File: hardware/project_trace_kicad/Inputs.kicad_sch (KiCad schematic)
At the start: 41 parts, among them J201 Conn_01x01_Socket, J202 Conn_01x01_Socket, J203 Conn_01x01_Socket, J204 Screw_Terminal_01x04, J205 Conn_Coaxial, U201 TLE2426xLP, U202 AQW280SX, U203 AQW282SX, U204 OPA2837IRUNT, U205 TS5A23159DGS, U206 OPA2837IRUNT

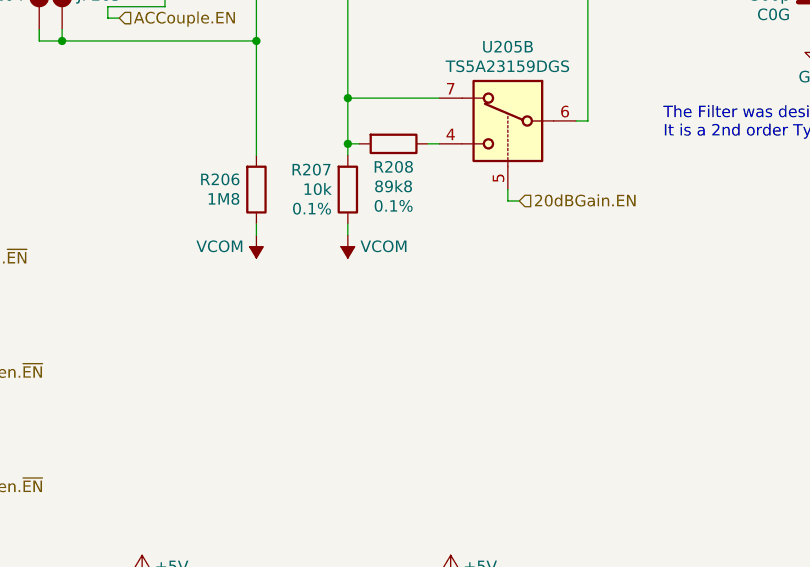
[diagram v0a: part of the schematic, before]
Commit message: Fix Bug in Diffamp, update PCB
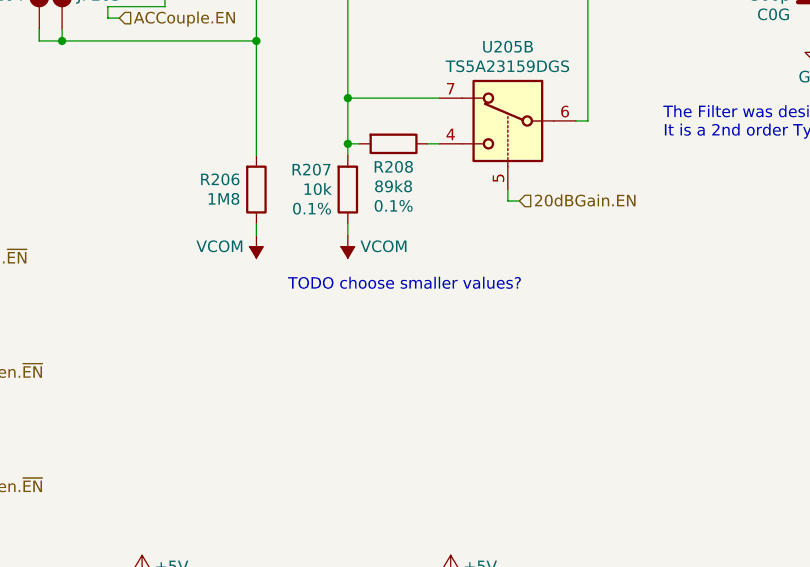
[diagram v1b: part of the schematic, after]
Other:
- note added: "TODO choose smaller values?"
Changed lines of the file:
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@@
+		)
+	)
+	(text "TODO choose smaller values?"
+		(exclude_from_sim no)
+		(at 186.69 102.108 0)
+		(effects
+			(font
+				(size 1.27 1.27)
+			)
 		)
 	)

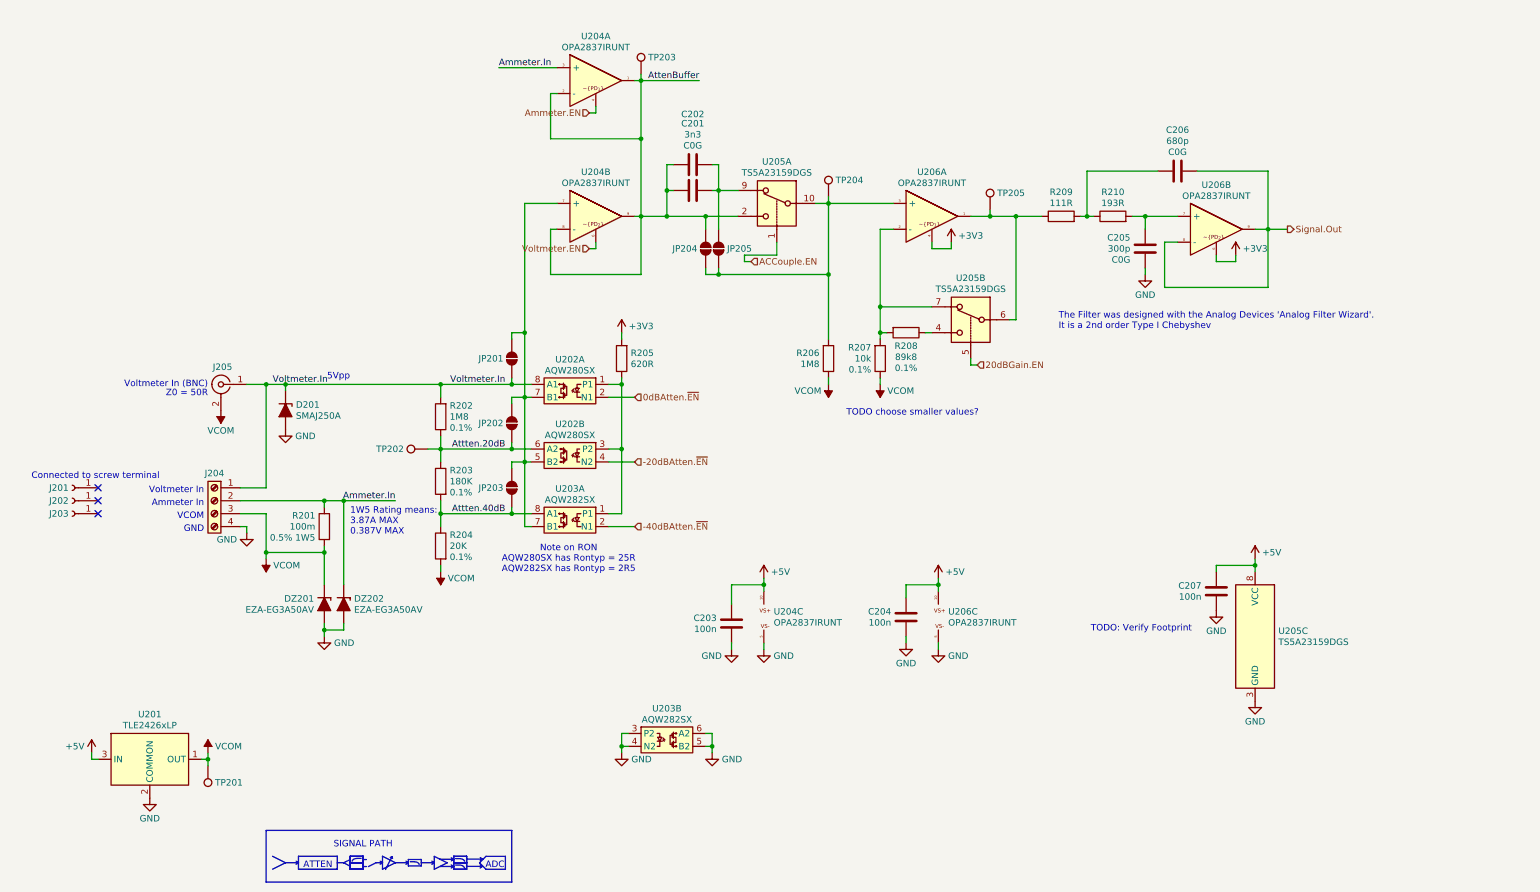
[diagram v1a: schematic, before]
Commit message: Work on PCB, Fix bugs, Improve noise performance
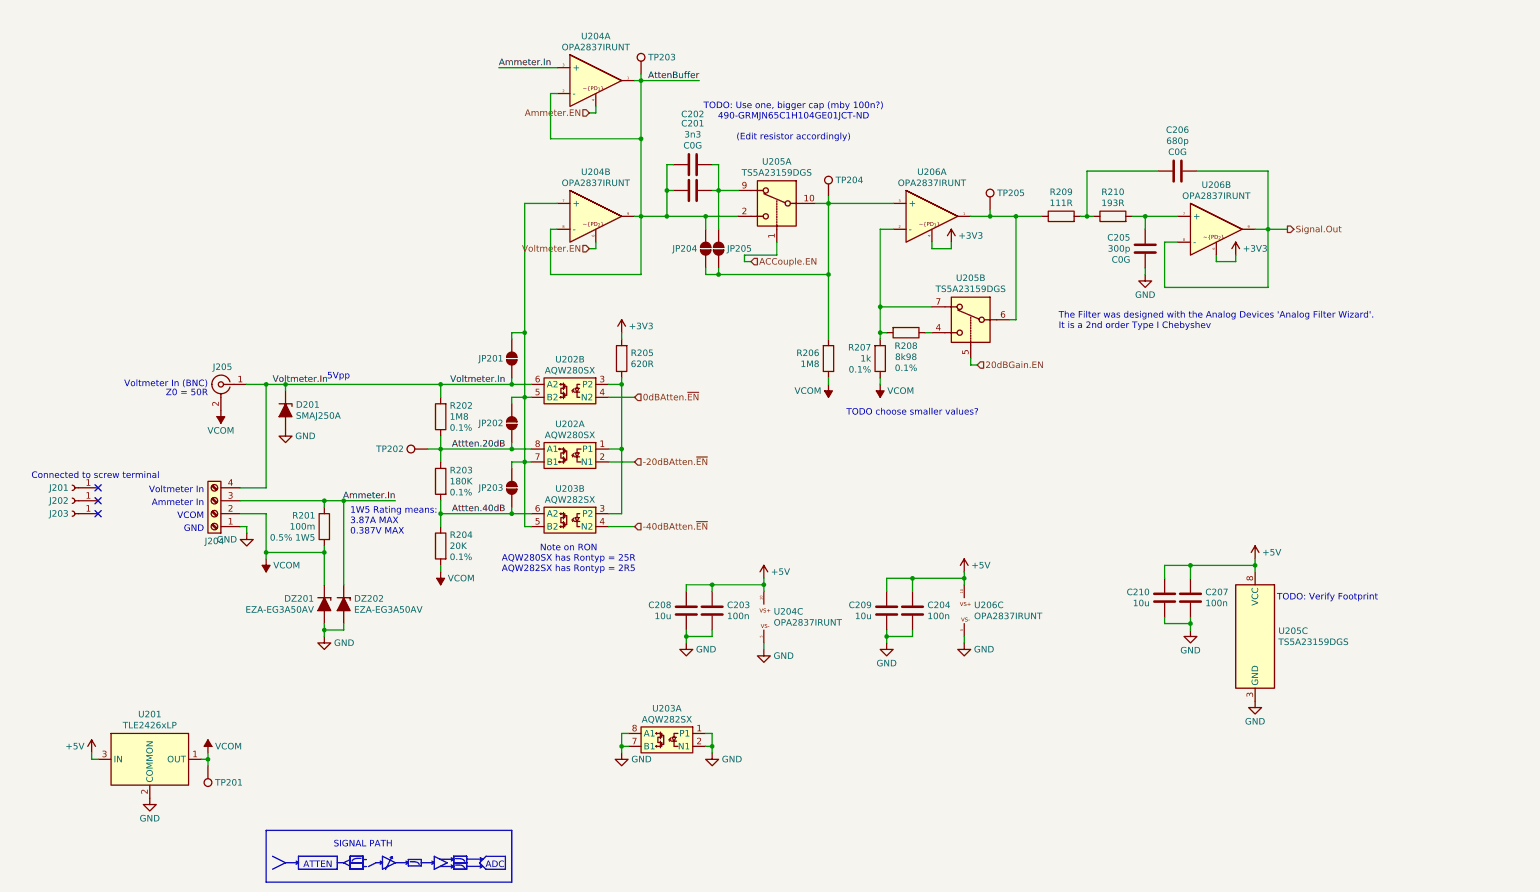
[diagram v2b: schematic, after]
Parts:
- added C208, C209, C210: 10u, Capacitor_SMD:C_0805_2012Metric_Pad1.18x1.45mm_HandSolder, symbol Device:C
- R207: value 10k -> 1k; DigikeyPN YAG1236CT-ND -> (none)
- R208: value 89k8 -> 8k98; DigikeyPN YAG1236CT-ND -> (none)
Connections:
- net +5V: now also C208.2, C209.2, C210.2
- net -20dBAtten.~{EN}: now also U202.2 (N1); no longer U202.4 (N2)
- net -40dBAtten.~{EN}: now also U203.4 (N2); no longer U203.2 (N1)
- net 0dBAtten.~{EN}: now also U202.4 (N2); no longer U202.2 (N1)
- net Ammeter.In: now also J204.3 (Pin_3); no longer J204.2 (Pin_2)
- net Attten.20dB: now also U202.8 (A1); no longer U202.6 (A2)
- net Attten.40dB: now also U203.6 (A2); no longer U203.8 (A1)
- net GND: now also J204.1 (Pin_1), U203.1 (P1), U203.2 (N1), U203.7 (B1), U203.8 (A1), C208.1, C209.1, C210.1; no longer J204.4 (Pin_4), U203.3 (P2), U203.4 (N2), U203.5 (B2), U203.6 (A2)
- net VCOM: now also J204.2 (Pin_2); no longer J204.3 (Pin_3)
- net Voltmeter.In: now also J204.4 (Pin_4), U202.6 (A2); no longer J204.1 (Pin_1), U202.8 (A1)
- net at R205.1, U202.1 (P1), U202.3 (P2): now also U203.3 (P2); no longer U203.1 (P1)
- net at JP201.2 (B), JP202.2 (B), JP203.2 (B)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: now also U203.5 (B2); no longer U203.7 (B1)
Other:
- note added: "TODO: Use one, bigger cap (mby 100n?) 490-GRMJN65C1H104GE01JCT-ND (Edit resistor accordingly)"
- moved on the sheet: C203, C204, C207, J204, U202A, U202B, U203A, U203B, U206C

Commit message: Layout Broad Strokes, Fix STM32H7 Error
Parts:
- added C211: 10u, Capacitor_SMD:C_0805_2012Metric_Pad1.18x1.45mm_HandSolder, symbol Device:C
- added C212: 100n, Capacitor_SMD:C_0603_1608Metric_Pad1.08x0.95mm_HandSolder, symbol Device:C
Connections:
- net +5V: now also C211.2, C212.1
- net 20dBGain.EN: now also U205.1; no longer U205.5
- net ACCouple.EN: now also U205.5; no longer U205.1
- net AttenBuffer: now also U205.4; no longer U205.2
- net GND: now also C211.1, C212.2
- net at JP204.2 (B), JP205.2 (B), TP204.1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: now also U205.6; no longer R206.2, U205.10
- net at R209.1, TP205.1, U206.1: now also U205.10; no longer U205.6
- net at R207.2, R208.2, U206.2 (-): now also U205.9; no longer U205.7
- net at R208.1: now also U205.2; no longer U205.4
- net at C201.2, C202.2, JP205.1 (A): now also R206.2, U205.7; no longer U205.9
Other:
- moved on the sheet: R206, U205A, U205B

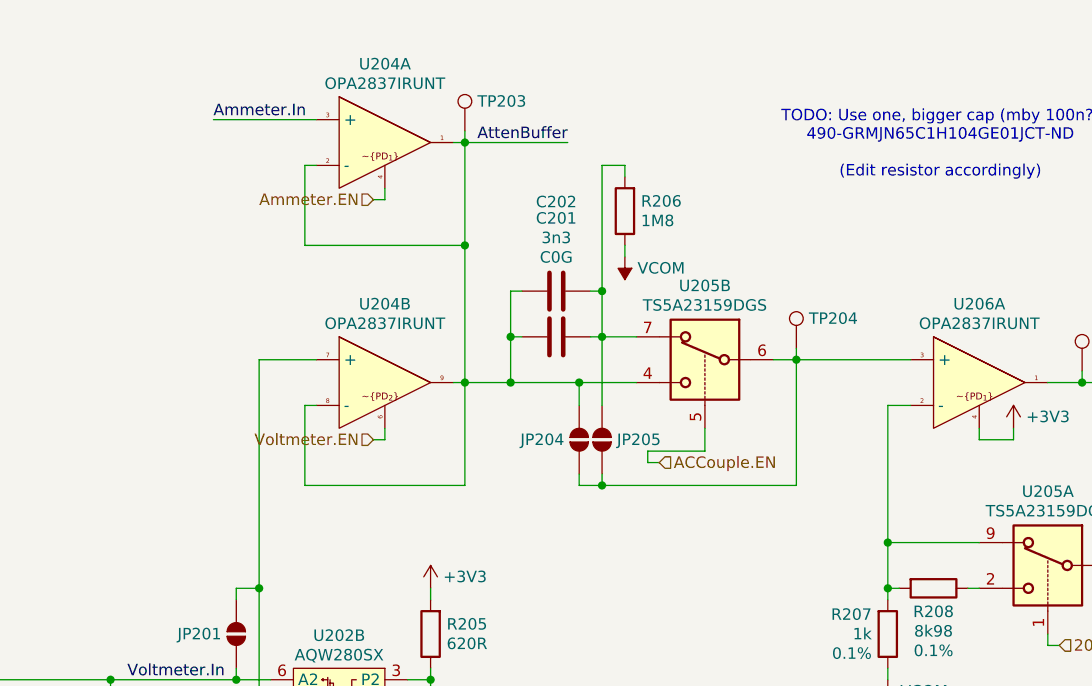
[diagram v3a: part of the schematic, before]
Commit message: Add missing Part-numers, Revise AC Coupling
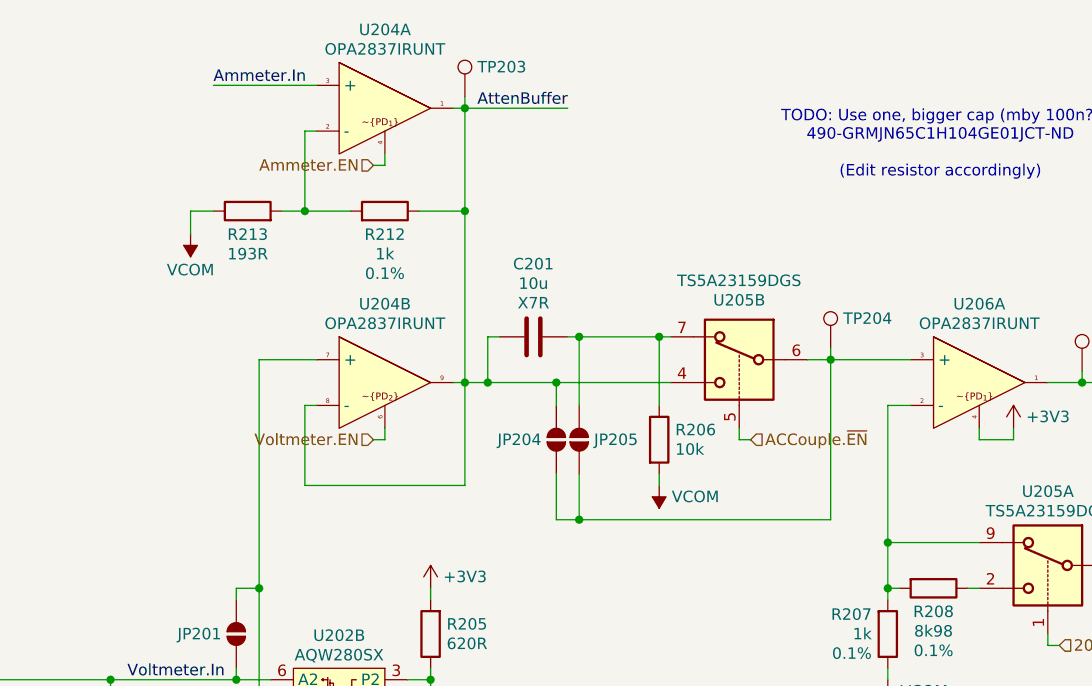
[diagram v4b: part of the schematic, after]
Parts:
- removed C202: 3n3, Capacitor_SMD:C_0603_1608Metric_Pad1.08x0.95mm_HandSolder, symbol Device:C
- added R212: 1k, Resistor_SMD:R_0603_1608Metric_Pad0.98x0.95mm_HandSolder, symbol Device:R
- added R213: 193R, Resistor_SMD:R_0603_1608Metric_Pad0.98x0.95mm_HandSolder, symbol Device:R
- C201: value 3n3 -> 10u; footprint Capacitor_SMD:C_0603_1608Metric_Pad1.08x0.95mm_HandSolder -> Capacitor_SMD:C_0805_2012Metric_Pad1.18x1.45mm_HandSolder; DigikeyPN 490-GCM1885C1H332FA16DCT-ND -> 490-10516-1-ND; Extra C0G -> X7R
- C205: DigikeyPN (none) -> 311-3967-1-ND
- C206: DigikeyPN (none) -> 311-1425-1-ND
- R206: value 1M8 -> 10k; footprint Resistor_SMD:R_0805_2012Metric_Pad1.20x1.40mm_HandSolder -> Resistor_SMD:R_0603_1608Metric_Pad0.98x0.95mm_HandSolder; DigikeyPN 408-2026-1-ND -> YAG1236CT-ND; Extra 0.1% -> (none)
- R207: DigikeyPN (none) -> YAG1237CT-ND
- R208: DigikeyPN (none) -> 13-RT0603BRD078K98LCT-ND
- R209: DigikeyPN (none) -> 2019-RN73R1JTTD1110B25CT-ND
- R210: DigikeyPN (none) -> 13-RT0603DRE07193RLCT-ND
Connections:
- net AttenBuffer: now also C201.2, R212.1; no longer C201.1, U204.2 (-)
- net VCOM: now also R206.2, R213.1; no longer R206.1
- net at JP205.1 (A), U205.7: now also C201.1, R206.1; no longer C201.2, R206.2
- net ACCouple.EN renamed ACCouple.~{EN}
- new net: R212.2, R213.2, U204.2 (-)
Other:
- moved on the sheet: JP204, JP205, TP203, TP204, U204A, U205B

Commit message: Address Review Comments
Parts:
- added C202: 4u7, Capacitor_THT:CP_Radial_D6.3mm_P2.50mm, symbol Device:C_Polarized
- added C213: 100n, Capacitor_SMD:C_0603_1608Metric_Pad1.08x0.95mm_HandSolder, symbol Device:C
- added U207: SN74LVC2G14DBV, Package_TO_SOT_SMD:SOT-23-6_Handsoldering, symbol 74xGxx:SN74LVC2G14DBV
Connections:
- net Ammeter.EN: now also U207.6 (1Y)
- net GND: now also C202.2, C213.2, U207.2 (GND), U207.3 (2A)
- net VCOM: now also C202.1
- net Voltmeter.EN: now also U207.1 (1A)
- new net: C213.1, U207.5 (V_{CC})
- no-connect marks 3 -> 4
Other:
- note added: "AC/DC Coupling"
- note added: "ADC has its nyquist frequency at 20MHz as it uses oversampling and a digital anti-aliasing filter."
- note added: "Attenuator"
- note added: "Sallen-Key Antialiasing Filter"
- note added: "Switchable Gain Amplifier"
- note added: "TODO: Connect new ammeter.en"
- note removed: "TODO: Use one, bigger cap (mby 100n?) 490-GRMJN65C1H104GE01JCT-ND (Edit resistor accordingly)"
- moved on the sheet: TP201

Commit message: Updates to PCB, Schematic Fixes
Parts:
- U207: DigikeyPN (none) -> 296-13010-1-ND
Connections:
- net +3V3: now also C213.1, U207.5 (V_{CC})
- net Voltmeter.EN renamed VOLT/~{AMP}
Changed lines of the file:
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@@
 	)
 	(junction
+		(at 67.31 31.75)
+		(diameter 0)
+		(color 0 0 0 0)
+	)
+	(junction
 		(at 129.54 167.64)
 		(diameter 0)
@@
 	(wire
 		(pts
-			(xy 105.41 30.48) (xy 116.84 30.48)
+			(xy 102.87 30.48) (xy 116.84 30.48)
 		)
 		(stroke
@@
 	(wire
 		(pts
-			(xy 124.46 69.85) (xy 124.46 68.58)
+			(xy 124.46 71.12) (xy 124.46 68.58)
 		)
 		(stroke
@@
 	(wire
 		(pts
-			(xy 124.46 39.37) (xy 124.46 38.1)
+			(xy 124.46 38.1) (xy 124.46 41.91)
 		)
 		(stroke
@@
 	(wire
 		(pts
-			(xy 123.19 69.85) (xy 124.46 69.85)
+			(xy 123.19 71.12) (xy 124.46 71.12)
 		)
 		(stroke
@@
 	(wire
 		(pts
+			(xy 67.31 30.48) (xy 67.31 31.75)
+		)
+		(stroke
+			(width 0)
+			(type default)
+		)
+	)
+	(wire
+		(pts
 			(xy 182.88 66.04) (xy 180.34 66.04)
 		)
@@
 	(wire
 		(pts
+			(xy 102.87 41.91) (xy 124.46 41.91)
+		)
+		(stroke
+			(width 0)
+			(type default)
+		)
+	)
+	(wire
+		(pts
 			(xy 129.54 168.91) (xy 129.54 167.64)
 		)
@@
 	(wire
 		(pts
-			(xy 124.46 39.37) (xy 123.19 39.37)
-		)
-		(stroke
-			(width 0)
-			(type default)
-		)
-	)
-	(wire
-		(pts
 			(xy 107.95 96.52) (xy 111.76 96.52)
 		)
@@
 		)
 	)
+	(label "Ammeter.EN"
+		(at 102.87 41.91 0)
+		(effects
+			(font
+				(size 1.27 1.27)
+			)
+			(justify left bottom)
+		)
+	)
 	(label "Ammeter.In"
 		(at 85.09 119.38 180)
@@
 	)
 	(label "Ammeter.In"
-		(at 105.41 30.48 0)
+		(at 102.87 30.48 0)
 		(effects
 			(font
@@
 		)
 	)
-	(hierarchical_label "Ammeter.EN"
-		(shape input)
-		(at 123.19 39.37 180)
-		(effects
-			(font
-				(size 1.27 1.27)
-			)
-			(justify right)
-		)
-	)
 	(hierarchical_label "-40dBAtten.~{EN}"
 		(shape input)
@@
 		)
 	)
-	(hierarchical_label "Voltmeter.EN"
-		(shape input)
-		(at 123.19 69.85 180)
-		(effects
-			(font
-				(size 1.27 1.27)
-			)
-			(justify right)
-		)
-	)
 	(hierarchical_label "Signal.Out"
 		(shape output)
@@
 		)
 	)
-	(hierarchical_label "Voltmeter.EN"
+	(hierarchical_label "VOLT{slash}~{AMP}"
+		(shape input)
+		(at 123.19 71.12 180)
+		(effects
+			(font
+				(size 1.27 1.27)
+			)
+			(justify right)
+		)
+	)
+	(hierarchical_label "VOLT{slash}~{AMP}"
 		(shape input)
 		(at 55.88 50.8 180)
@@
 			)
 		)
+		(property "DigikeyPN" "296-13010-1-ND"
+			(at 67.31 53.34 0)
+			(hide yes)
+			(show_name no)
+			(do_not_autoplace no)
+			(effects
+				(font
+					(size 1.27 1.27)
+				)
+			)
+		)
 		(pin "5"
 		)
@@
 				)
 			)
+		)
+	)
+	(symbol
+		(lib_id "power:+3V3")
+		(at 67.31 30.48 0)
+		(unit 1)
+		(body_style 1)
+		(exclude_from_sim no)
+		(in_bom yes)
+		(on_board yes)
+		(in_pos_files yes)
+		(dnp no)
+		(fields_autoplaced yes)
+		(property "Reference" "#PWR0233"
+			(at 67.31 34.29 0)
+			(hide yes)
+			(show_name no)
+			(do_not_autoplace no)
+			(effects
+				(font
+					(size 1.27 1.27)
+				)
+			)
+		)
+		(property "Value" "+3V3"
+			(at 67.31 26.4752 0)
+			(show_name no)
+			(do_not_autoplace no)
+			(effects
+				(font
+					(size 1.27 1.27)
+				)
+			)
+		)
+		(property "Footprint" ""
+			(at 67.31 30.48 0)
+			(hide yes)
+			(show_name no)
+			(do_not_autoplace no)
+			(effects
+				(font
+					(size 1.27 1.27)
+				)
+			)
+		)
+		(property "Datasheet" ""
+			(at 67.31 30.48 0)
+			(hide yes)
+			(show_name no)
+			(do_not_autoplace no)
+			(effects
+				(font
+					(size 1.27 1.27)
+				)
+			)
+		)
+		(property "Description" "Power symbol creates a global label with name \"+3V3\""
+			(at 67.31 30.48 0)
+			(hide yes)
+			(show_name no)
+			(do_not_autoplace no)
+			(effects
+				(font
+					(size 1.27 1.27)
+				)
+			)
+		)
+		(pin "1"
+		)
+		(instances
+			(project "project_trace_kicad"
+				(path "/af51f4e5-b952-4b0e-baf2-78a72fb86fcd/9b26f668-c4b4-4b55-bc2a-8936f081d498"
+					(reference "#PWR0233")
+					(unit 1)
+				)
+			)
